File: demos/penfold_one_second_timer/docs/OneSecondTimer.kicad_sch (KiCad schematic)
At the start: 12 parts

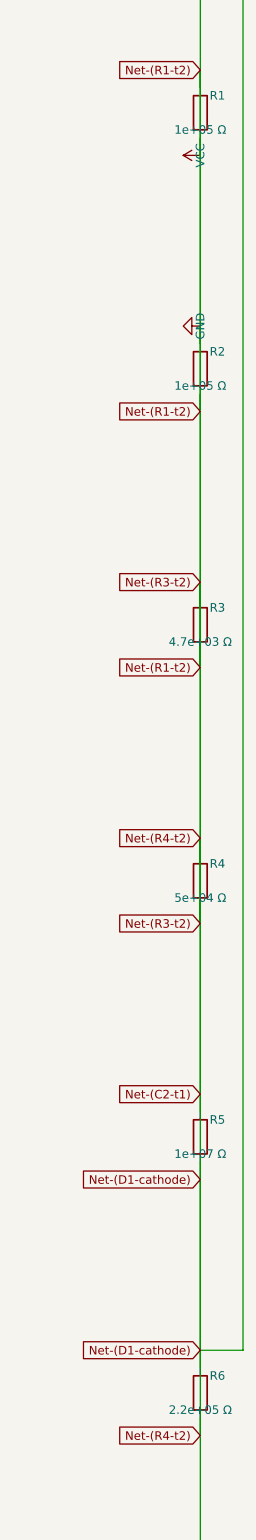
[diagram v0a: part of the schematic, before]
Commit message: units: Ohms.__str__ uses engineering notation (kΩ, MΩ, GΩ)
The previous `Ohms.__str__` formatted with bare `:.3g`, producing
unreadable scientific output for clean kilo / mega multiples:

  str(Ohms(10_000))     == "1e+04 Ω"      → now "10 kΩ"
  str(Ohms(100_000))    == "1e+05 Ω"      → now "100 kΩ"
  str(Ohms(1_000_000))  == "1e+06 Ω"      → now "1 MΩ"

The breadboard SVG visualiser surfaced the problem: a resistor body
labelled "100000Ω" makes a reader count zeros, while a label of
"100 kΩ" reads at a glance — exactly the convention every schematic
and parts catalogue uses. Centralising the engineering notation in
`Ohms.__str__` means every downstream consumer (assembly guide,
breadboard SVG, kicad netlist, BOM, reports) inherits the readable
form without each format adapter rolling its own formatter.

  - `Ohms.__str__` returns "47 Ω", "4.7 kΩ", "10 kΩ", "100 kΩ",
    "1 MΩ", "10 MΩ", "1 GΩ" per the kilo / mega / giga thresholds.
  - `Resistor.__str__` delegates to `str(self._ohms)` so it
    inherits the new notation (was producing the noisy "47.0 Ω"
    via raw float).
  - The breadboard visualiser's resistor body label uses
    `str(part.ohms)` directly (previously had a private
    `_format_ohms_compact` helper; removed).
  - `tests/components/test_resistor.py::test_str` updated for
    "47 Ω" (was "47.0 Ω"); new `test_str_renders_in_engineering_notation`
    pins kΩ / MΩ output across the kilo and mega thresholds.
  - All demo docs / goldens refreshed where the Ohms.__str__
    change affected the rendered output (breadboard SVGs, kicad
    sch value fields, BOM rows).
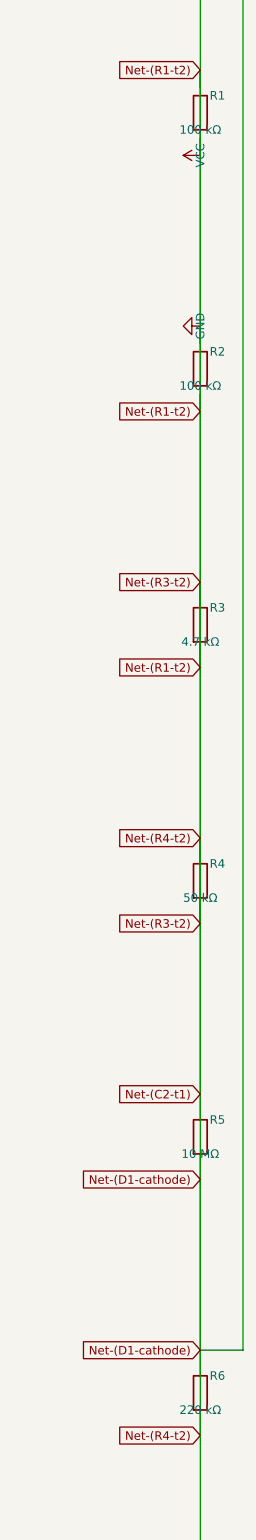
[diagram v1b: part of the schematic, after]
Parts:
- R1, R2: value 1e+05 Ω -> 100 kΩ
- R3: value 4.7e+03 Ω -> 4.7 kΩ
- R4: value 5e+04 Ω -> 50 kΩ
- R5: value 1e+07 Ω -> 10 MΩ
- R6: value 2.2e+05 Ω -> 220 kΩ
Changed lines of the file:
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@@
       (effects (font (size 1.27 1.27)))
     )
-    (property "Value" "1e+05 Ω"
+    (property "Value" "100 kΩ"
       (at 63.5 180.34 0)
       (effects (font (size 1.27 1.27)))
@@
       (effects (font (size 1.27 1.27)))
     )
-    (property "Value" "1e+05 Ω"
+    (property "Value" "100 kΩ"
       (at 63.5 218.44 0)
       (effects (font (size 1.27 1.27)))
@@
       (effects (font (size 1.27 1.27)))
     )
-    (property "Value" "4.7e+03 Ω"
+    (property "Value" "4.7 kΩ"
       (at 63.5 256.54 0)
       (effects (font (size 1.27 1.27)))
@@
       (effects (font (size 1.27 1.27)))
     )
-    (property "Value" "5e+04 Ω"
+    (property "Value" "50 kΩ"
       (at 63.5 294.64 0)
       (effects (font (size 1.27 1.27)))
@@
       (effects (font (size 1.27 1.27)))
     )
-    (property "Value" "1e+07 Ω"
+    (property "Value" "10 MΩ"
       (at 63.5 332.74 0)
       (effects (font (size 1.27 1.27)))
@@
       (effects (font (size 1.27 1.27)))
     )
-    (property "Value" "2.2e+05 Ω"
+    (property "Value" "220 kΩ"
       (at 63.5 370.84 0)
       (effects (font (size 1.27 1.27)))

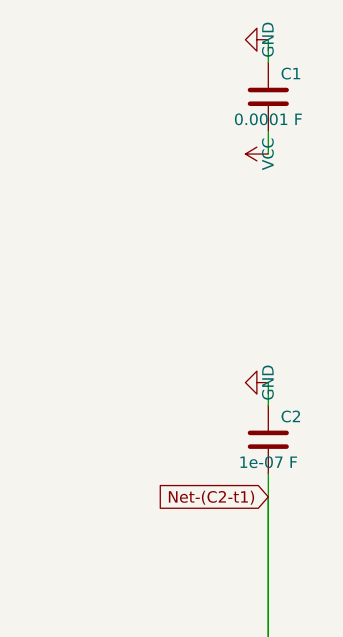
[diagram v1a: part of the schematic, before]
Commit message: units: Farads + Henries __str__ also use engineering notation
Same treatment as `Ohms.__str__` (previous commit) for the other two
passive engineering quantities. Demos contain caps and inductors
with values that the bare `:.3g` formatter would emit in scientific
form (`1e-07 F` for a 100 nF decoupling cap); centralising the
engineering notation on the unit class means every consumer
(reports, BOM, breadboard SVG, etc.) inherits the readable form.

  - `Farads.__str__` returns `100 pF`, `22 nF`, `100 nF`, `1 µF`,
    `4.7 µF`, `470 µF`, `1 mF`, `1 F` across the standard
    capacitance bands.
  - `Henries.__str__` returns `100 nH`, `10 µH`, `22 mH`, `1 H`
    across the standard inductance bands.
  - `Capacitor.__str__` and `Inductor.__str__` delegate to the
    unit class's str (were rolling raw-float formatters).
  - `framework.export.reports_common.part_description` now uses
    `str(part.ohms / farads / henries)` directly instead of the
    parallel `_format_ohms` / `_format_farads` / `_format_henries`
    helpers (removed — they duplicated the new logic on raw
    floats).
  - Breadboard SVG renderer now also labels capacitor and inductor
    bodies with their engineering-notation value (was only
    resistors).
  - `tests/framework/test_units.py`: parametrised regression tests
    for both unit classes across every band.
  - All affected demo docs / goldens refreshed.
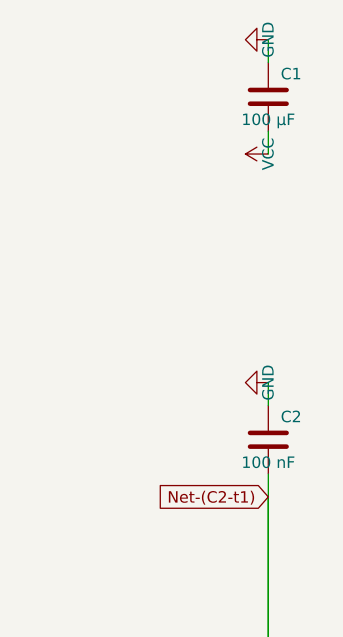
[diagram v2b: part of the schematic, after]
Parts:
- C1: value 0.0001 F -> 100 µF
- C2: value 1e-07 F -> 100 nF
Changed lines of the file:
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@@
       (effects (font (size 1.27 1.27)))
     )
-    (property "Value" "1e-07 F"
+    (property "Value" "100 nF"
       (at 63.5 66.04 0)
       (effects (font (size 1.27 1.27)))
@@
       (effects (font (size 1.27 1.27)))
     )
-    (property "Value" "0.0001 F"
+    (property "Value" "100 µF"
       (at 63.5 27.94 0)
       (effects (font (size 1.27 1.27)))
